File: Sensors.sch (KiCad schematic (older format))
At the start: 50 parts, among them CON1 CONSOLE, P1 CONN_02X20, P10 CBUS, P11 I2C0, P12 I2C0, P13 I2C1, P14 I2C1, P7 96B_SPI, Q2 CJ2305, Q3 CJ2305, SW1 VIO, U1 CJT1117-3.3, U2 XC6206, U3 FT230XS, U4 TXB0108PW, U5 TXS0108E

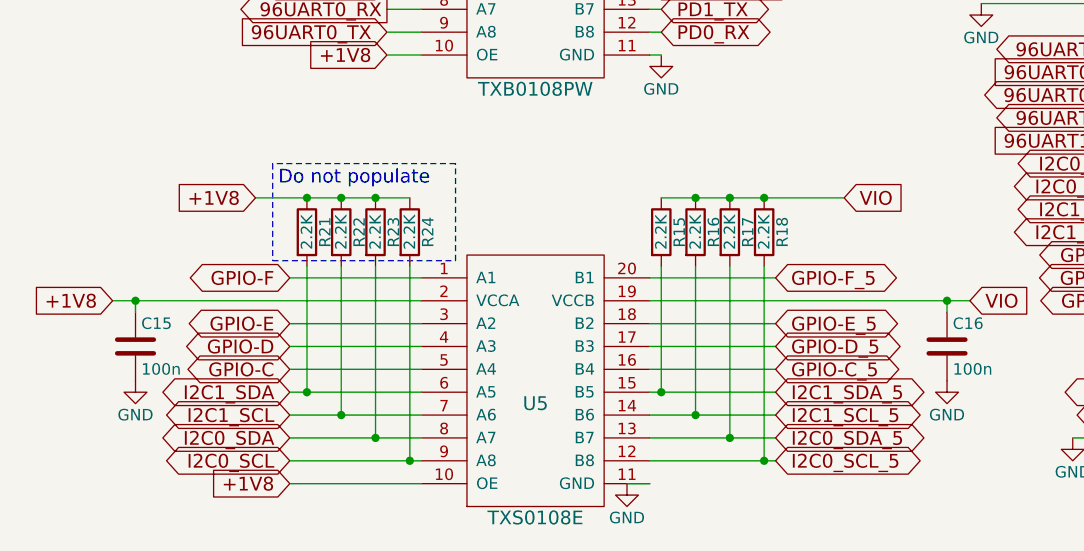
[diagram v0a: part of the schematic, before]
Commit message: Remove i2c pullups and add 22 ohm series resistors to reduce noise
There have been all kinds of problems with noise on the i2c bus, but the
pull up strength seems to be just fine for the bus speed that we're
using. Remove the pull up resistors, but put in series resistors to
reduce the effects of crosstalk on the i2c lines.

Also, split the data and clock signals so they don't run parallel across
the whole board. That should also reduce noise.

Signed-off-by: Grant Likely <grant.likely@linaro.org>
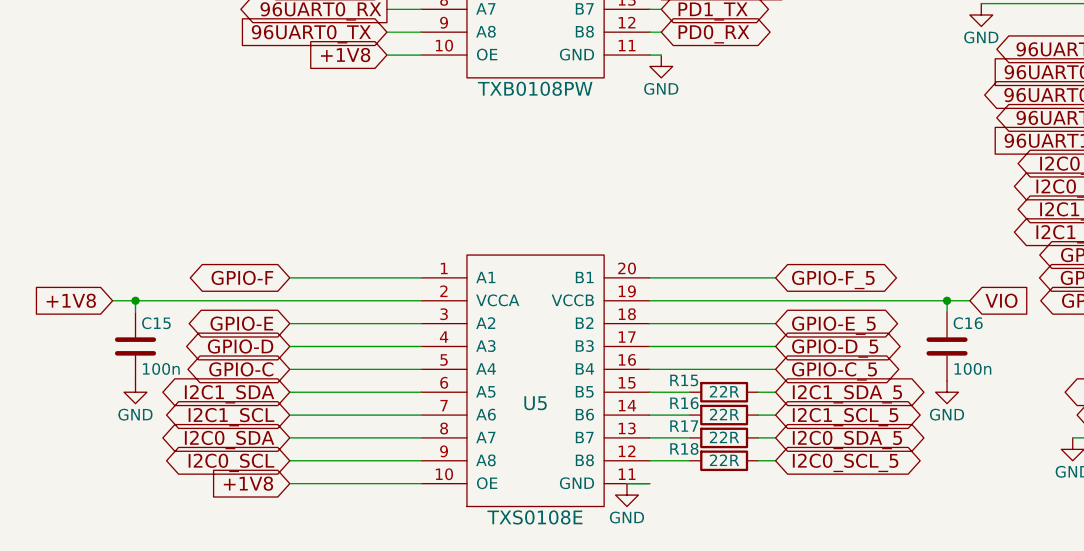
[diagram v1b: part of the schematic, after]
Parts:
- removed R21, R22, R23, R24: 2.2K, Sensors:R_0603_Seeed, symbol R
- R15, R16, R17, R18: value 2.2K -> 22R; Mfr YAGEO -> (none); Mfr Part # RC0603JR-072K2L -> (none); Seeed SKU 301010124 -> (none)
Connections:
- net I2C0_SCL_5: now also R18.1; no longer R18.2, U5.12 (B8)
- net I2C0_SDA_5: now also R17.1; no longer R17.2, U5.13 (B7)
- net I2C1_SCL_5: now also R16.1; no longer R16.2, U5.14 (B6)
- net I2C1_SDA_5: now also R15.1; no longer R15.2, U5.15 (B5)
- net VIO: no longer R15.1, R16.1, R17.1, R18.1
- new net: R18.2, U5.12 (B8)
- new net: R17.2, U5.13 (B7)
- new net: R16.2, U5.14 (B6)
- new net: R15.2, U5.15 (B5)
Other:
- note removed: "Do not populate"
- moved on the sheet: R15, R16, R17, R18

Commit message: Update testplan and manufacturing files for revB
Ready for manufacturing (finally!)

Signed-off-by: Grant Likely <grant.likely@linaro.org>
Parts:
- R15, R16, R17, R18: Mfr (none) -> Yageo; Mfr Part # (none) -> RC0603JR-0722RL; Seeed SKU (none) -> 301010289
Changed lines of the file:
@@
 F 2 "Sensors:R_0603_Seeed" V 3505 7200 30  0001 C CNN
 F 3 "" H 3575 7200 30  0000 C CNN
+F 4 "301010289" H 2400 3100 60  0001 C CNN "Seeed SKU"
+F 5 "Yageo" H 2400 3100 60  0001 C CNN "Mfr"
+F 6 "RC0603JR-0722RL" H 2400 3100 60  0001 C CNN "Mfr Part #"
 	1    3575 7200
 	0    1    1    0
@@
 F 2 "Sensors:R_0603_Seeed" V 3505 7300 30  0001 C CNN
 F 3 "" H 3575 7300 30  0000 C CNN
+F 4 "301010289" H 2400 3100 60  0001 C CNN "Seeed SKU"
+F 5 "Yageo" H 2400 3100 60  0001 C CNN "Mfr"
+F 6 "RC0603JR-0722RL" H 2400 3100 60  0001 C CNN "Mfr Part #"
 	1    3575 7300
 	0    1    1    0
@@
 F 2 "Sensors:R_0603_Seeed" V 3505 7400 30  0001 C CNN
 F 3 "" H 3575 7400 30  0000 C CNN
+F 4 "301010289" H 2400 3100 60  0001 C CNN "Seeed SKU"
+F 5 "Yageo" H 2400 3100 60  0001 C CNN "Mfr"
+F 6 "RC0603JR-0722RL" H 2400 3100 60  0001 C CNN "Mfr Part #"
 	1    3575 7400
 	0    1    1    0
@@
 F 2 "Sensors:R_0603_Seeed" V 3505 7500 30  0001 C CNN
 F 3 "" H 3575 7500 30  0000 C CNN
+F 4 "301010289" H 2400 3100 60  0001 C CNN "Seeed SKU"
+F 5 "Yageo" H 2400 3100 60  0001 C CNN "Mfr"
+F 6 "RC0603JR-0722RL" H 2400 3100 60  0001 C CNN "Mfr Part #"
 	1    3575 7500
 	0    1    1    0

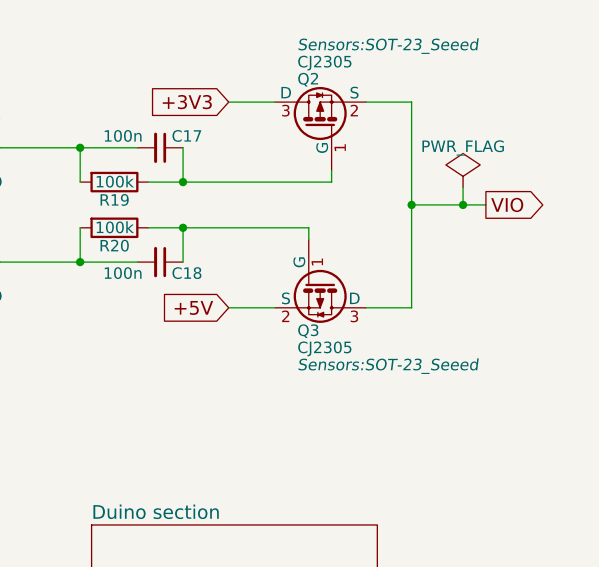
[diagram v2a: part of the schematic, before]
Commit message: Add 10uF to VIO power rail
I'm a little worried about noise on the power rail. Add a 10uF cap to
really make sure the rail is clean.

Signed-off-by: Grant Likely <grant.likely@linaro.org>
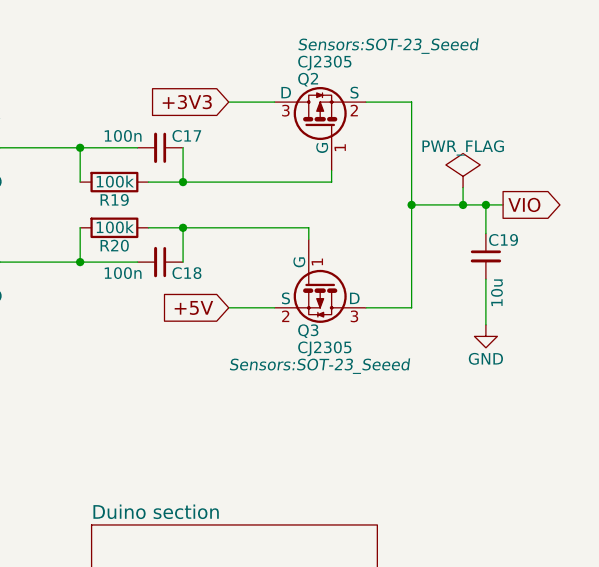
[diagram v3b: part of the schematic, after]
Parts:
- added C19: 10u, Capacitors_SMD:C_0805, symbol C_Small
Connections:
- net GND: now also C19.2
- net VIO: now also C19.1
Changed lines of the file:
@@
 	0    1    1    0
 $EndComp
-Text GLabel 10875 1600 2    60   Output ~ 0
+Text GLabel 10950 1600 2    60   Output ~ 0
 VIO
 Text GLabel 7950 1600 0    60   Input ~ 0
@@
 F 0 "Q3" V 10350 1850 50  0000 L CNN
 F 1 "CJ2305" V 10425 1850 50  0000 L CNN
-F 2 "Sensors:SOT-23_Seeed" V 10500 1850 50  0000 L CIN
+F 2 "Sensors:SOT-23_Seeed" V 10500 1550 50  0000 L CIN
 F 3 "" H 10150 1950 50  0000 L CNN
 F 4 "305030014" H 10150 1950 60  0001 C CNN "Seeed SKU"
@@
 	10550 1150 10550 2050
 Wire Wire Line
-	10550 1600 10875 1600
+	10550 1600 10950 1600
 Wire Wire Line
 	10550 2050 10350 2050
@@
 Wire Wire Line
 	3725 7500 3800 7500
+$Comp
+L C_Small C19
+U 1 1 563FD0E5
+P 10875 1825
+F 0 "C19" H 10885 1895 50  0000 L CNN
+F 1 "10u" V 10925 1600 50  0000 L CNN
+F 2 "Capacitors_SMD:C_0805" H 10875 1825 60  0001 C CNN
+F 3 "" H 10875 1825 60  0000 C CNN
+F 4 "302010178" H 10875 1825 60  0001 C CNN "Seeed SKU"
+F 5 "YAGEO" H 10875 1825 60  0001 C CNN "Mfr"
+F 6 "CC0805KKX5R8BB106" H 10875 1825 60  0001 C CNN "Mfr Part #"
+	1    10875 1825
+	1    0    0    -1
+$EndComp
+Wire Wire Line
+	10875 1725 10875 1600
+Connection ~ 10875 1600
+Wire Wire Line
+	10875 2125 10875 1925
+$Comp
+L GND #PWR032
+U 1 1 563FE2D2
+P 10875 2125
+F 0 "#PWR032" H 10875 1875 50  0001 C CNN
+F 1 "GND" H 10875 1975 50  0000 C CNN
+F 2 "" H 10875 2125 60  0000 C CNN
+F 3 "" H 10875 2125 60  0000 C CNN
+	1    10875 2125
+	1    0    0    -1
+$EndComp
 $EndSCHEMATC

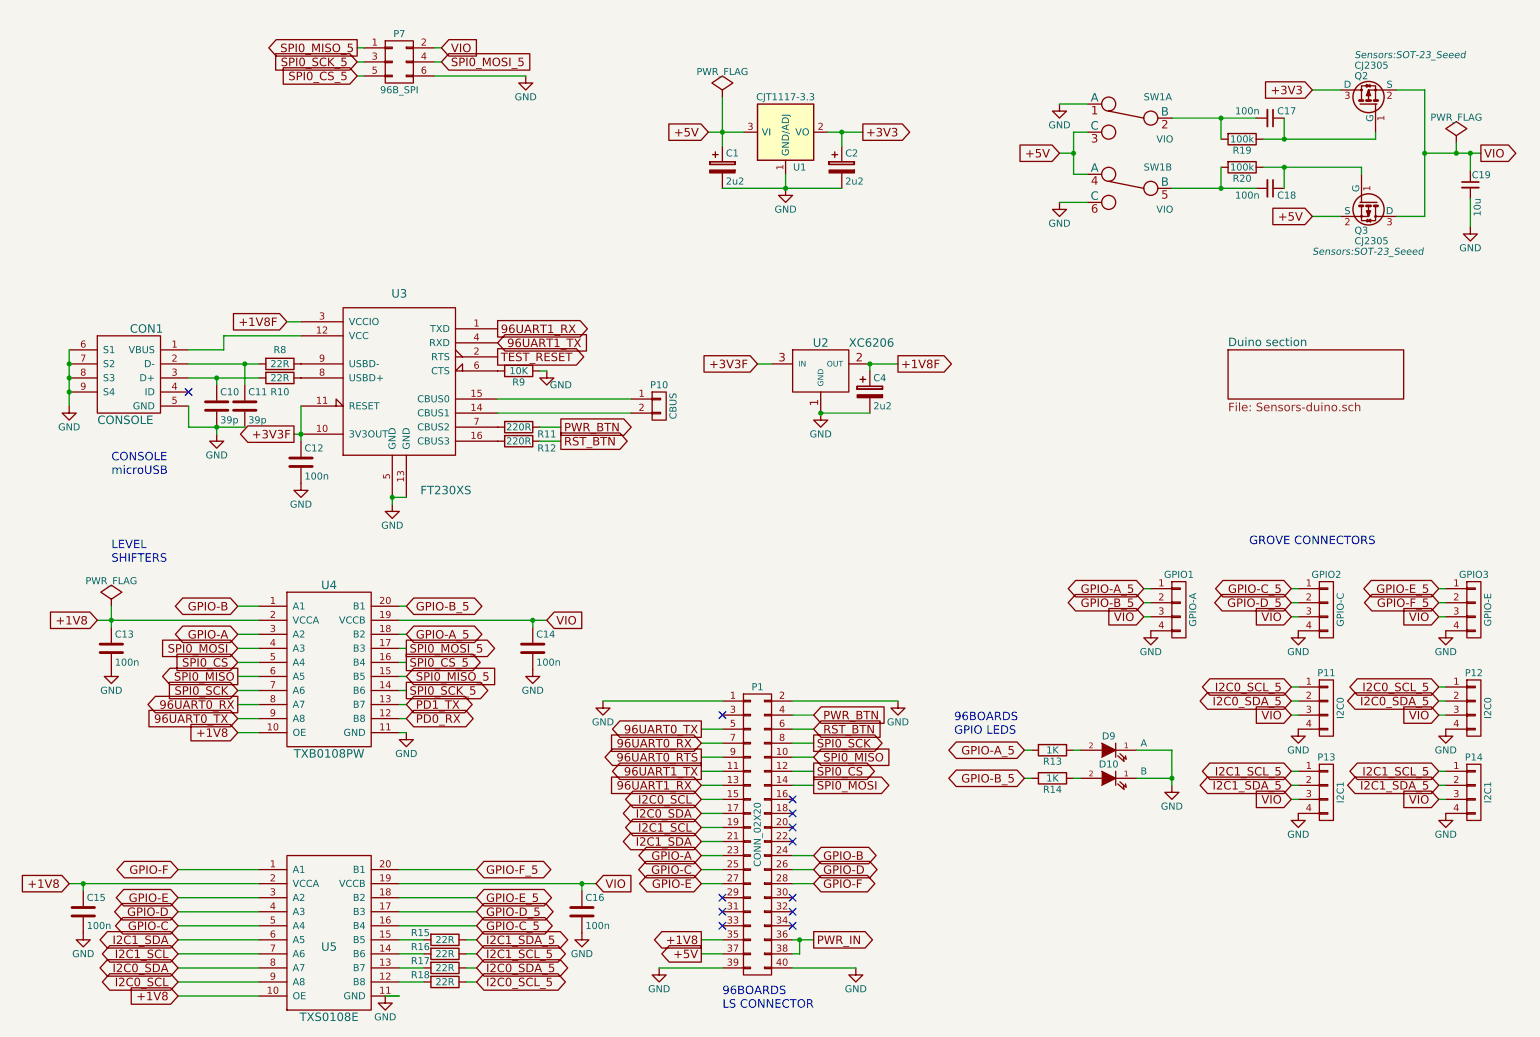
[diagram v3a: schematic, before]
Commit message: Replace TXS0108 level shifters for i2c with PCA9306
The TXS0108 doesn't work well with long trace lengths on i2c. When there
is too much capacitive load on the line the integrated one-shot drivers
go into oscillation and it locks up the bus. Since we cannot make the
TXS0108 work reliably, use a different part on the i2c lines. The
PCA9306 is a simpler circuit without the one-shot driver and it works
reliably on a prototyped bread-board circuit.

Sadly, the PCA9306 takes up a lot more room because it doesn't have
integrated pull-up resistors, and there wasn't any more room on the
board to place the new parts. Drop the switchable voltage levels to get
back some space at the top of the board where the shifters need to be.
Instead, hardwire each I2C bus at a different voltage level. I2C0 is
shifted to 5V, and I2C1 to 3.3V. Fix the ATMEGA to 5V only. GPIO-A and
GPIO-B are shifted to 5V, and GPIOs E-L are shifted to 3.3V (5V
tolerant). We don't use GPIOs C & D.

Finally, the 96B GPIOs and I2C grove connectors have swapped sides to
make routing easier.

Signed-off-by: Grant Likely <grant.likely@linaro.org>
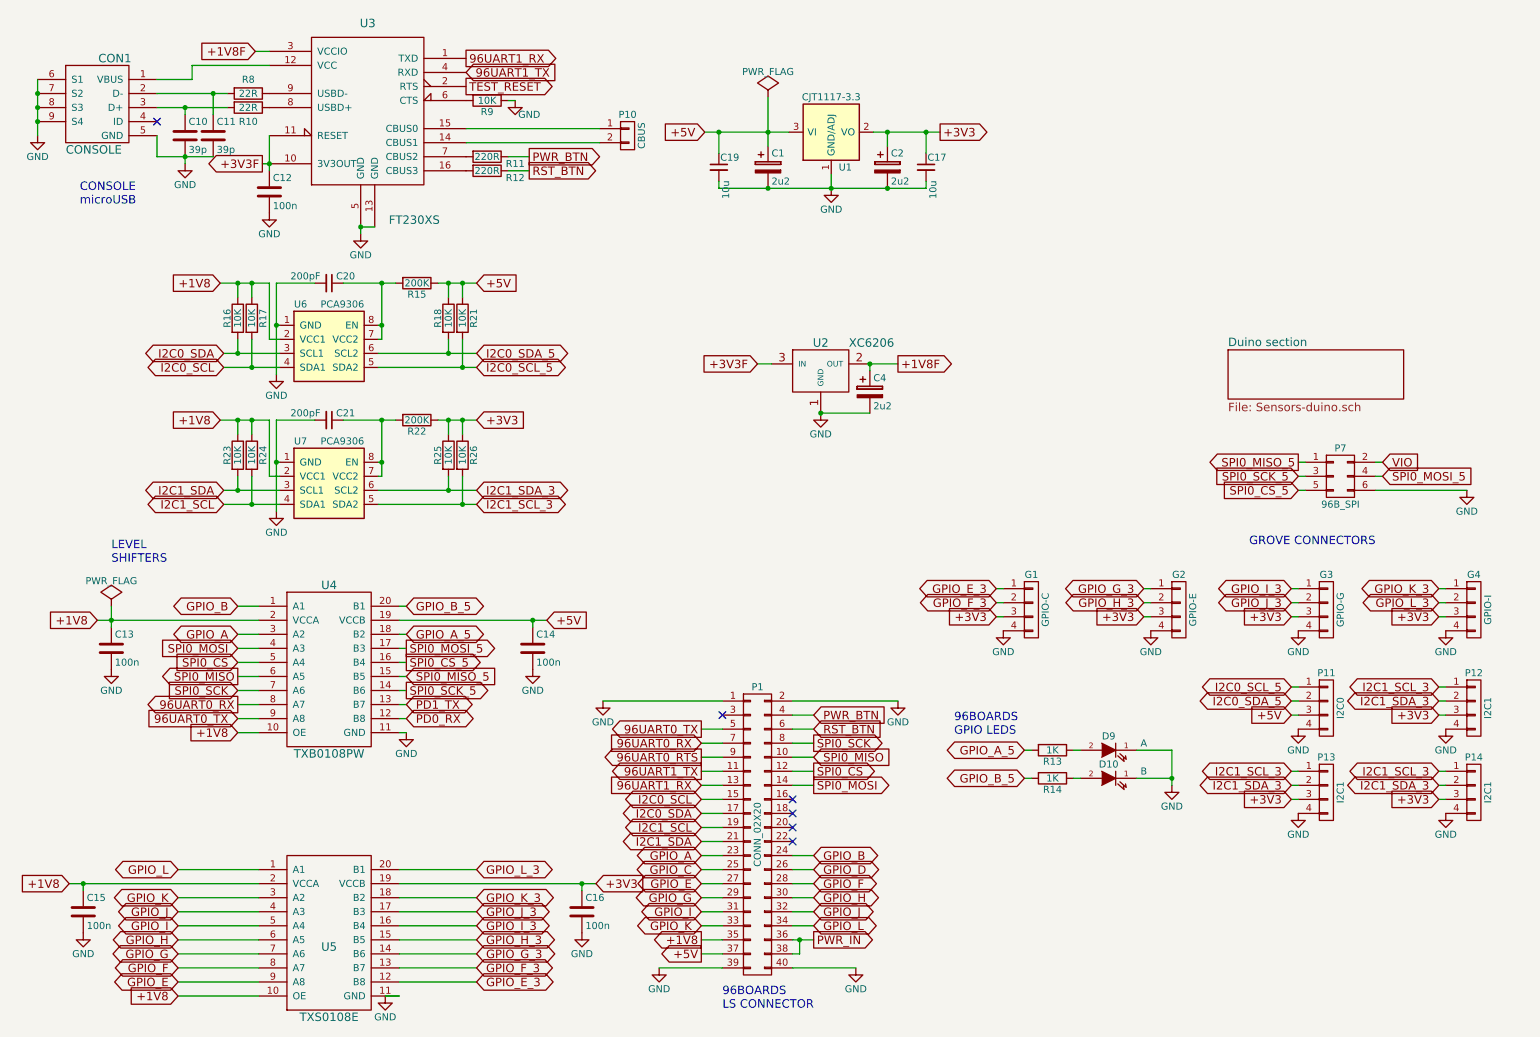
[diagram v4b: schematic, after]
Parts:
- removed C18: 100n, Capacitors_SMD:C_0603, symbol C_Small
- removed Q2, Q3: CJ2305, Sensors:SOT-23_Seeed, symbol CJ2305
- removed R19, R20: 100k, Sensors:R_0603_Seeed, symbol R
- removed SW1: VIO, Sensors:DIP_Toggle_Switch, symbol Switch_SPDT_x2
- added C20, C21: 200pF, Capacitors_SMD:C_0603, symbol C_Small
- added G4: GPIO-I, Sensors:Grove4P, symbol CONN_01X04
- added R21, R23, R24, R25, R26: 10K, Sensors:R_0603_Seeed, symbol R
- added R22: 200K, Sensors:R_0603_Seeed, symbol R
- added U6, U7: PCA9306, Sensors:VSSOP-8_2.4x2.1mm_Pitch0.5mm, symbol PCA9306
- C17: value 100n -> 10u; footprint Capacitors_SMD:C_0603 -> Capacitors_SMD:C_0805; Mfr Yageo -> YAGEO; Mfr Part # CC0603KRX7R9BB104 -> CC0805KKX5R8BB106; Seeed SKU 302010138 -> 302010178
- G1: renamed from GPIO1; value GPIO-A -> GPIO-C
- G2: renamed from GPIO2; value GPIO-C -> GPIO-E
- G3: renamed from GPIO3; value GPIO-E -> GPIO-G
- P12: value I2C0 -> I2C1
- R15: value 22R -> 200K; Mfr Yageo -> (none); Mfr Part # RC0603JR-0722RL -> (none); Seeed SKU 301010289 -> (none)
- R16, R17, R18: value 22R -> 10K; Mfr Yageo -> (none); Mfr Part # RC0603JR-0722RL -> (none); Seeed SKU 301010289 -> (none)
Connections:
- net +1V8: now also R16.1, R17.1, R23.1, R24.1, U6.2 (VCC1), U7.2 (VCC1)
- net +3V3: now also C16.1, C17.1, G1.3 (P3), G2.3 (P3), G3.3 (P3), P12.3 (P3), P13.3 (P3), P14.3 (P3), U5.19 (VCCB), G4.3 (P3), R22.1, R25.1, R26.1
- net +5V: now also C14.1, C19.1, P11.3 (P3), R15.1, R18.1, U4.19 (VCCB), R21.1
- net GND: now also C17.2, C20.2, C21.2, G4.4 (P4), U6.1 (GND), U7.1 (GND)
- net I2C0_SCL: now also R17.2, U6.4 (SDA1); no longer U5.9 (A8)
- net I2C0_SCL_5: now also R21.2, U6.5 (SDA2); no longer P12.1 (P1), R18.1
- net I2C0_SDA: now also R16.2, U6.3 (SCL1); no longer U5.8 (A7)
- net I2C0_SDA_5: now also R18.2, U6.6 (SCL2); no longer P12.2 (P2), R17.1
- net I2C1_SCL: now also R24.2, U7.4 (SDA1); no longer U5.7 (A6)
- net I2C1_SDA: now also R23.2, U7.3 (SCL1); no longer U5.6 (A5)
- net VIO: no longer C14.1, C16.1, C19.1, G1.3 (P3), G2.3 (P3), G3.3 (P3), P11.3 (P3), P12.3 (P3), P13.3 (P3), P14.3 (P3), U4.19 (VCCB), U5.19 (VCCB)
- net GPIO_G: now reaches P1.29 (P29)
- net GPIO_G: now also U5.7 (A6)
- net GPIO_H: now reaches P1.30 (P30)
- net GPIO_H: now also U5.6 (A5)
- net GPIO_I: now reaches P1.31 (P31)
- net GPIO_I: now also U5.5 (A4)
- net GPIO_J: now reaches P1.32 (P32)
- net GPIO_J: now also U5.4 (A3)
- net GPIO_K: now reaches P1.33 (P33)
- net GPIO_K: now also U5.3 (A2)
- net GPIO_L: now reaches P1.34 (P34)
- net GPIO_L: now also U5.1 (A1)
- net GPIO_E_3: now reaches U5.12 (B8)
- net GPIO_E_3: now also G1.1 (P1); no longer R18.2
- net GPIO_F_3: now reaches U5.13 (B7)
- net GPIO_F_3: now also G1.2 (P2); no longer R17.2
- net GPIO_G_3: now reaches U5.14 (B6)
- net GPIO_G_3: now also G2.1 (P1); no longer R16.2
- net at R15.2: now also C20.1, U6.7 (VCC2), U6.8 (EN); no longer U5.15 (B5)
- net GPIO-A renamed GPIO_A
- net GPIO-A_5 renamed GPIO_A_5
- net GPIO_A_5: no longer G1.1 (P1)
- net GPIO-B renamed GPIO_B
- net GPIO-B_5 renamed GPIO_B_5
- net GPIO_B_5: no longer G1.2 (P2)
- net GPIO-C renamed GPIO_C
- net GPIO_C: no longer U5.5 (A4)
- net GPIO-C_5 renamed GPIO_I_3
- net GPIO_I_3: now also G3.1 (P1); no longer G2.1 (P1)
- net GPIO-D renamed GPIO_D
- net GPIO_D: no longer U5.4 (A3)
- net GPIO-D_5 renamed GPIO_H_3
- net GPIO_H_3: now also U5.15 (B5); no longer U5.17 (B3)
- net GPIO-E renamed GPIO_E
- net GPIO_E: now also U5.9 (A8); no longer U5.3 (A2)
- net GPIO-E_5 renamed GPIO_K_3
- net GPIO_K_3: now also G4.1 (P1); no longer G3.1 (P1)
- net GPIO-F renamed GPIO_F
- net GPIO_F: now also U5.8 (A7); no longer U5.1 (A1)
- net GPIO-F_5 renamed GPIO_J_3
- net GPIO_J_3: now also U5.17 (B3); no longer U5.20 (B1)
- net I2C1_SCL_5 renamed I2C1_SCL_3
- net I2C1_SCL_3: now also P12.1 (P1), R26.2, U7.5 (SDA2); no longer R16.1
- net I2C1_SDA_5 renamed I2C1_SDA_3
- net I2C1_SDA_3: now also P12.2 (P2), R25.2, U7.6 (SCL2); no longer R15.1
- new net: C21.1, R22.2, U7.7 (VCC2), U7.8 (EN)
- new net GPIO_L_3: G4.2 (P2), U5.20 (B1)
- no-connect marks 12 -> 6
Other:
- moved on the sheet: C1, C10, C11, C12, C19, C2, CON1, G1, G2, G3, P10, P7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
